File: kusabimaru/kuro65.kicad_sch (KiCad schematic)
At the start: 23 parts, among them IC1 ATMEGA32U4, J1 ISP, J2 USB4085-GF-A, SW1 SW_RESET, Y1 16MHz

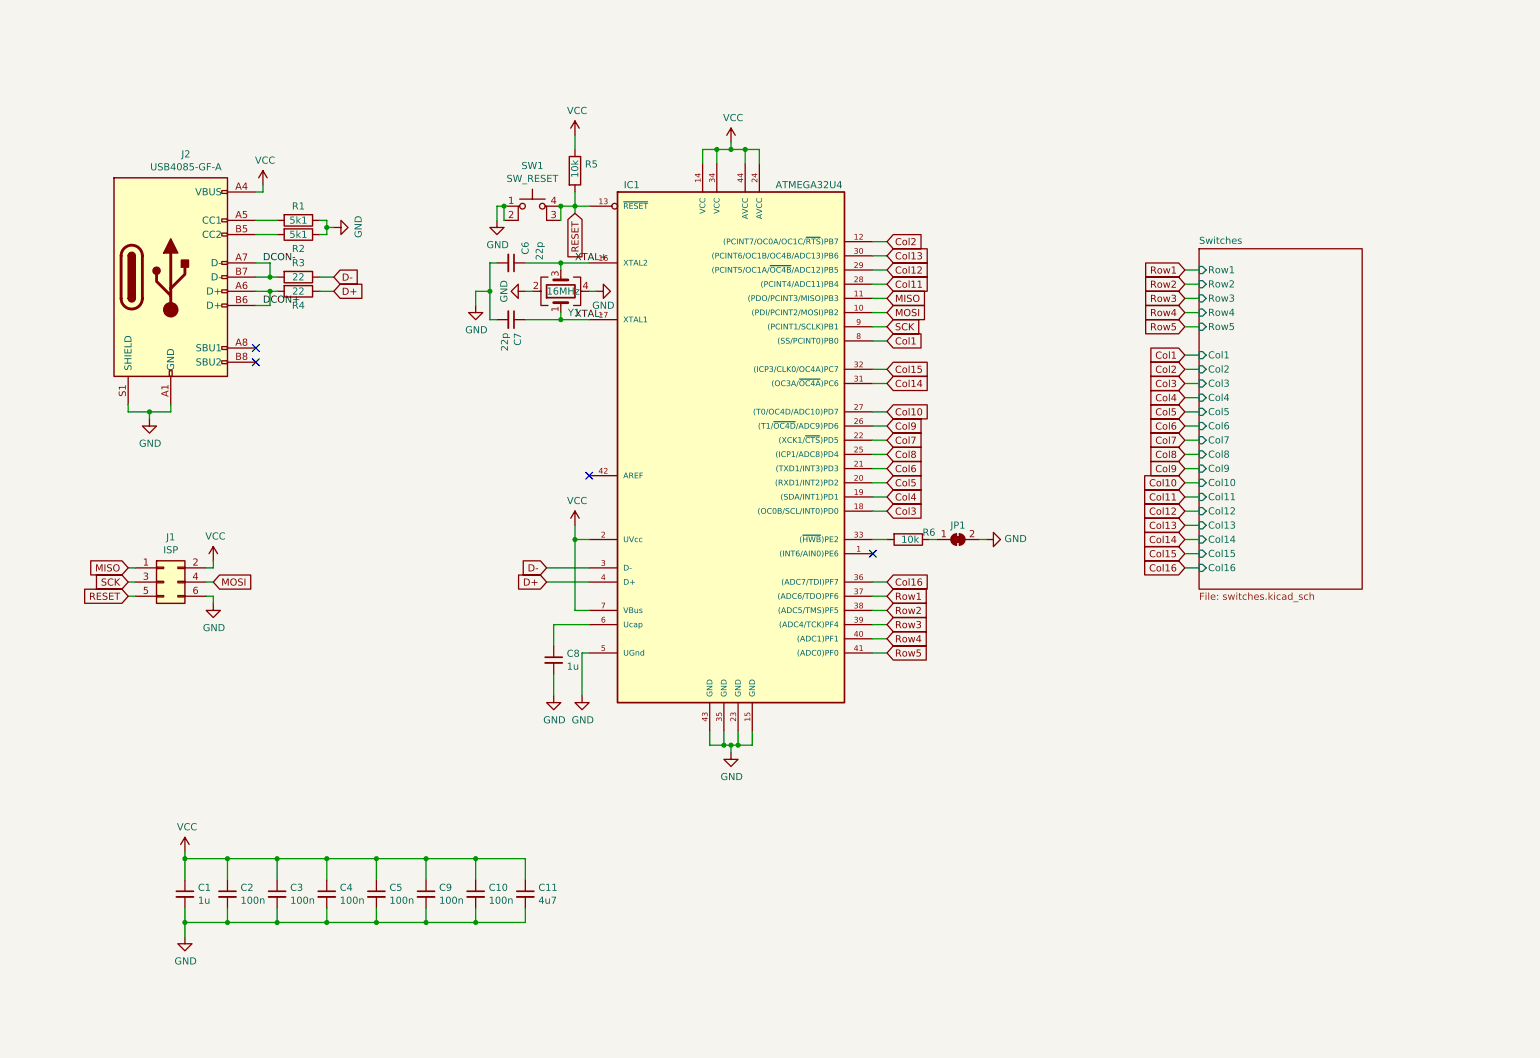
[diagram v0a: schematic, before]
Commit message: Changed schematic and PCB layout for kuro65. Routing of PCB is incomplete.
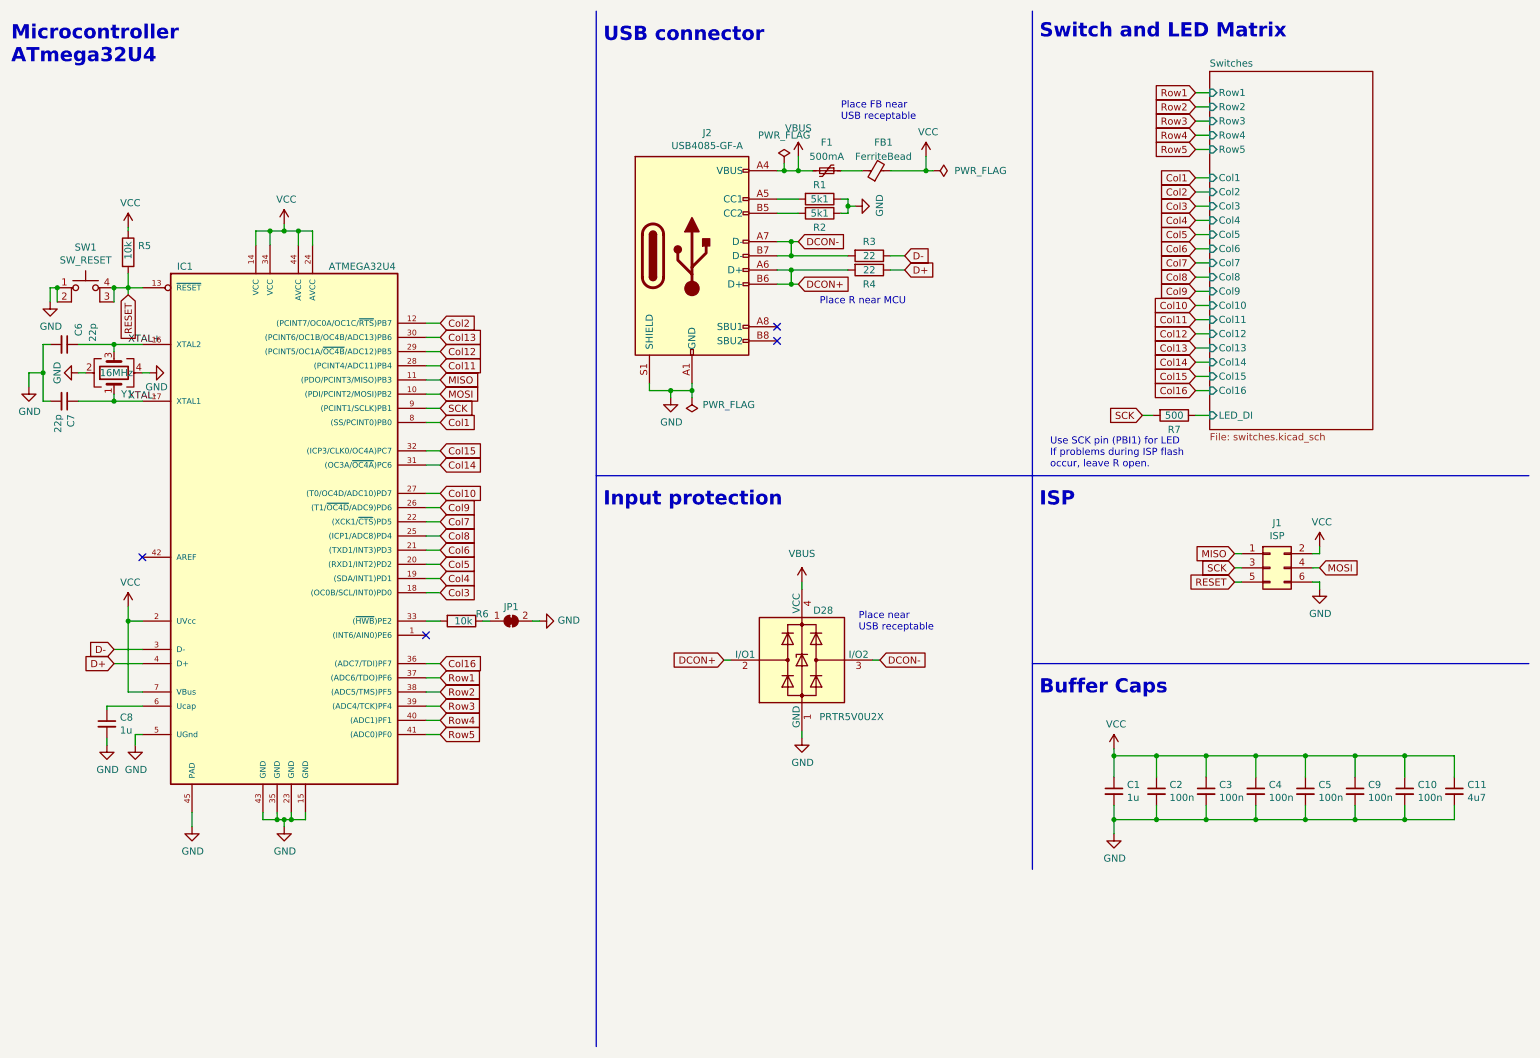
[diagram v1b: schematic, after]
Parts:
- added D28: PRTR5V0U2X, Package_TO_SOT_SMD:SOT-143, symbol Power_Protection:PRTR5V0U2X
- added F1: 500mA, Fuse:Fuse_0603_1608Metric_Pad1.05x0.95mm_HandSolder, symbol Device:Polyfuse_Small
- added FB1: FerriteBead, Resistor_SMD:R_0805_2012Metric_Pad1.20x1.40mm_HandSolder, symbol Device:FerriteBead_Small
- added R7: 500, Resistor_SMD:R_0603_1608Metric_Pad0.98x0.95mm_HandSolder, symbol Device:R
- C1, C10, C11, C2, C3, C4, C5, C6, C7, C8, C9: footprint Capacitor_SMD:C_0805_2012Metric_Pad1.18x1.45mm_HandSolder -> Capacitor_SMD:C_0603_1608Metric_Pad1.08x0.95mm_HandSolder
- IC1: footprint Package_QFP:TQFP-44_10x10mm_P0.8mm -> TM_qfn:QFN-44-1EP_7x7mm_P0.5mm_EP5.2x5.2mm_hand_solder
- R1, R2, R3, R4, R5, R6: footprint Resistor_SMD:R_0805_2012Metric_Pad1.20x1.40mm_HandSolder -> Resistor_SMD:R_0603_1608Metric_Pad0.98x0.95mm_HandSolder
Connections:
- net DCON+: now also D28.2 (I/O1)
- net DCON-: now also D28.3 (I/O2)
- net GND: now also IC1.45 (PAD), D28.1 (GND)
- net SCK: now also R7.2
- net VCC: now also FB1.2; no longer J2.A4 (VBUS), J2.A9 (VBUS), J2.B4 (VBUS), J2.B9 (VBUS)
- new net: F1.1, FB1.1
- new net Switches/LED_DI: R7.1
- new net VBUS: D28.4 (VCC), F1.2, J2.A4 (VBUS), J2.A9 (VBUS), J2.B4 (VBUS), J2.B9 (VBUS)
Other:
- sheet Switches ports: added LED_DI; removed none
- note added: "Buffer Caps"
- note added: "ISP"
- note added: "Input protection"
- note added: "Microcontroller ATmega32U4"
- note added: "Place FB near USB receptable"
- note added: "Place R near MCU"
- note added: "Place near USB receptable"
- note added: "Switch and LED Matrix"
- note added: "USB connector"
- note added: "Use SCK pin (PBI1) for LED If problems during ISP flash occur, leave R open."
- moved on the sheet: C1, C10, C11, C2, C3, C4, C5, C6, C7, C8, C9, J1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

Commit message: Updated PCB layout for DZ65 compatibility.
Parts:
- added IC2: ATMEGA32U4, Package_QFP:LQFP-44_10x10mm_P0.8mm, symbol atmega32u4:ATMEGA32U4
- IC1: footprint TM_qfn:QFN-44-1EP_7x7mm_P0.5mm_EP5.2x5.2mm_hand_solder -> Package_DFN_QFN:QFN-44-1EP_7x7mm_P0.5mm_EP5.2x5.2mm_ThermalVias
- J2: value USB4085-GF-A -> USB TYPE-C-31-M-12; footprint Connector_USB:USB_C_Receptacle_GCT_USB4085 -> Connector_USB:USB_C_Receptacle_HRO_TYPE-C-31-M-12; Shop-URL https://www.digikey.de/product-detail/de/gct/USB4085-GF-A/2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 -> https://jlcpcb.com/partdetail/Korean_HropartsElec-TYPE_C_31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
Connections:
- net Col1: now also IC2.8 ((SS/PCINT0)PB0)
- net Col10: now also IC2.27 ((T0/OC4D/ADC10)PD7)
- net Col11: now also IC2.28 ((PCINT4/ADC11)PB4)
- net Col12: now also IC2.29 ((PCINT5/OC1A/~{OC4B}/ADC12)PB5)
- net Col13: now also IC2.30 ((PCINT6/OC1B/OC4B/ADC13)PB6)
- net Col14: now also IC2.31 ((OC3A/~{OC4A})PC6)
- net Col15: now also IC2.32 ((ICP3/CLK0/OC4A)PC7)
- net Col16: now also IC2.36 ((ADC7/TDI)PF7)
- net Col2: now also IC2.12 ((PCINT7/OC0A/OC1C/~{RTS})PB7)
- net Col3: now also IC2.18 ((OC0B/SCL/INT0)PD0)
- net Col4: now also IC2.19 ((SDA/INT1)PD1)
- net Col5: now also IC2.20 ((RXD1/INT2)PD2)
- net Col6: now also IC2.21 ((TXD1/INT3)PD3)
- net Col7: now also IC2.22 ((XCK1/~{CTS})PD5)
- net Col8: now also IC2.25 ((ICP1/ADC8)PD4)
- net Col9: now also IC2.26 ((T1/~{OC4D}/ADC9)PD6)
- net D+: now also IC2.4 (D+)
- net D-: now also IC2.3 (D-)
- net GND: now also IC2.15 (GND), IC2.23 (GND), IC2.35 (GND), IC2.43 (GND), IC2.45 (PAD), IC2.5 (UGnd)
- net MISO: now also IC2.11 ((PDO/PCINT3/MISO)PB3)
- net MOSI: now also IC2.10 ((PDI/PCINT2/MOSI)PB2)
- net RESET: now also IC2.13 (~{RESET})
- net Row1: now also IC2.37 ((ADC6/TDO)PF6)
- net Row2: now also IC2.38 ((ADC5/TMS)PF5)
- net Row3: now also IC2.39 ((ADC4/TCK)PF4)
- net Row4: now also IC2.40 ((ADC1)PF1)
- net Row5: now also IC2.41 ((ADC0)PF0)
- net SCK: now also IC2.9 ((PCINT1/SCLK)PB1)
- net VCC: now also IC2.14 (VCC), IC2.2 (UVcc), IC2.24 (AVCC), IC2.34 (VCC), IC2.44 (AVCC), IC2.7 (VBus)
- net XTAL+: now also IC2.16 (XTAL2)
- net XTAL-: now also IC2.17 (XTAL1)
- net at IC1.1 ((INT6/AIN0)PE6): now also IC2.1 ((INT6/AIN0)PE6)
- net at IC1.33 ((~{HWB})PE2), R6.2: now also IC2.33 ((~{HWB})PE2)
- net at IC1.42 (AREF): now also IC2.42 (AREF)
- net at C8.1, IC1.6 (Ucap): now also IC2.6 (Ucap)
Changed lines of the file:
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@@
     (company "0x544D")
   )
+  (junction (at 87.63 113.665) (diameter 0) (color 0 0 0 0)
+  )
+  (junction (at 87.63 128.905) (diameter 0) (color 0 0 0 0)
+  )
+  (junction (at 87.63 141.605) (diameter 0) (color 0 0 0 0)
+  )
   (junction (at 131.445 80.01) (diameter 0) (color 0 0 0 0)
   )
   (junction (at 59.69 51.435) (diameter 0) (color 0 0 0 0)
   )
+  (junction (at 87.63 136.525) (diameter 0) (color 0 0 0 0)
+  )
   (junction (at 62.23 156.845) (diameter 0) (color 0 0 0 0)
   )
@@
   (junction (at 236.22 145.415) (diameter 0) (color 0 0 0 0)
   )
+  (junction (at 87.63 139.065) (diameter 0) (color 0 0 0 0)
+  )
   (junction (at 135.255 80.01) (diameter 0) (color 0 0 0 0)
   )
   (junction (at 236.22 156.845) (diameter 0) (color 0 0 0 0)
   )
+  (junction (at 87.63 116.205) (diameter 0) (color 0 0 0 0)
+  )
   (junction (at 63.5 156.845) (diameter 0) (color 0 0 0 0)
   )
@@
   (junction (at 34.29 121.285) (diameter 0) (color 0 0 0 0)
   )
+  (junction (at 87.63 108.585) (diameter 0) (color 0 0 0 0)
+  )
   (junction (at 153.035 53.34) (diameter 0) (color 0 0 0 0)
   )
   (junction (at 254 145.415) (diameter 0) (color 0 0 0 0)
   )
+  (junction (at 87.63 131.445) (diameter 0) (color 0 0 0 0)
+  )
   (junction (at 31.75 61.595) (diameter 0) (color 0 0 0 0)
   )
+  (junction (at 87.63 121.285) (diameter 0) (color 0 0 0 0)
+  )
   (junction (at 21.59 61.595) (diameter 0) (color 0 0 0 0)
   )
@@
   (junction (at 227.33 145.415) (diameter 0) (color 0 0 0 0)
   )
+  (junction (at 87.63 133.985) (diameter 0) (color 0 0 0 0)
+  )
   (junction (at 153.035 58.42) (diameter 0) (color 0 0 0 0)
   )
   (junction (at 218.44 145.415) (diameter 0) (color 0 0 0 0)
   )
+  (junction (at 87.63 106.045) (diameter 0) (color 0 0 0 0)
+  )
   (junction (at 163.195 46.99) (diameter 0) (color 0 0 0 0)
   )
@@
   (junction (at 262.89 145.415) (diameter 0) (color 0 0 0 0)
   )
+  (junction (at 87.63 111.125) (diameter 0) (color 0 0 0 0)
+  )
   (junction (at 254 156.845) (diameter 0) (color 0 0 0 0)
   )
@@
     (property "Reference" "IC1" (id 0) (at 44.45 57.785 0))
     (property "Value" "ATMEGA32U4" (id 1) (at 76.2 57.785 0))
-    (property "Footprint" "TM_qfn:QFN-44-1EP_7x7mm_P0.5mm_EP5.2x5.2mm_hand_solder" (id 2) (at 74.93 154.94 0)
+    (property "Footprint" "Package_DFN_QFN:QFN-44-1EP_7x7mm_P0.5mm_EP5.2x5.2mm_ThermalVias" (id 2) (at 74.93 154.94 0)
       (effects (font (size 1.27 1.27)) hide)
     )
@@
     (in_bom yes) (on_board yes)
     (property "Reference" "J2" (id 0) (at 137.9728 33.8582 0))
-    (property "Value" "USB4085-GF-A" (id 1) (at 137.9728 36.1696 0))
-    (property "Footprint" "Connector_USB:USB_C_Receptacle_GCT_USB4085" (id 2) (at 139.065 55.88 0)
+    (property "Value" "USB TYPE-C-31-M-12" (id 1) (at 137.9728 36.1696 0))
+    (property "Footprint" "Connector_USB:USB_C_Receptacle_HRO_TYPE-C-31-M-12" (id 2) (at 139.065 55.88 0)
       (effects (font (size 1.27 1.27)) hide)
     )
@@
       (effects (font (size 1.27 1.27)) hide)
     )
-    (property "Shop-URL" "https://www.digikey.de/product-detail/de/gct/USB4085-GF-A/2073-USB4085-GF-ACT-ND/9859733" (id 4) (at 135.255 55.88 0)
+    (property "Shop-URL" "https://jlcpcb.com/partdetail/Korean_HropartsElec-TYPE_C_31_M12/C165948" (id 4) (at 135.255 55.88 0)
       (effects (font (size 1.27 1.27)) hide)
     )
@@
     (pin "1")
   )
+  (symbol (lib_id "atmega32u4:ATMEGA32U4") (at 62.23 104.775 0) (unit 1)
+    (in_bom yes) (on_board yes) (fields_autoplaced)
+    (property "Reference" "IC2" (id 0) (at 69.1897 53.34 0)
+      (effects (font (size 1.27 1.27)) (justify left))
+    )
+    (property "Value" "ATMEGA32U4" (id 1) (at 69.1897 55.88 0)
+      (effects (font (size 1.27 1.27)) (justify left))
+    )
+    (property "Footprint" "Package_QFP:LQFP-44_10x10mm_P0.8mm" (id 2) (at 74.93 154.94 0)
+      (effects (font (size 1.27 1.27)) hide)
+    )
+    (property "Datasheet" "" (id 3) (at 62.23 104.775 0)
+      (effects (font (size 1.27 1.27)) hide)
+    )
+    (pin "1")
+    (pin "10")
+    (pin "11")
+    (pin "12")
+    (pin "13")
+    (pin "14")
+    (pin "15")
+    (pin "16")
+    (pin "17")
+    (pin "18")
+    (pin "19")
+    (pin "2")
+    (pin "20")
+    (pin "21")
+    (pin "22")
+    (pin "23")
+    (pin "24")
+    (pin "25")
+    (pin "26")
+    (pin "27")
+    (pin "28")
+    (pin "29")
+    (pin "3")
+    (pin "30")
+    (pin "31")
+    (pin "32")
+    (pin "33")
+    (pin "34")
+    (pin "35")
+    (pin "36")
+    (pin "37")
+    (pin "38")
+    (pin "39")
+    (pin "4")
+    (pin "40")
+    (pin "41")
+    (pin "42")
+    (pin "43")
+    (pin "44")
+    (pin "45")
+    (pin "5")
+    (pin "6")
+    (pin "7")
+    (pin "8")
+    (pin "9")
+  )
   (symbol (lib_id "power:GND") (at 154.94 142.24 0) (unit 1)
     (in_bom yes) (on_board yes)
@@
     )
     (path "/00000000-0000-0000-0000-000060129e73"
-      (reference "IC1") (unit 1) (value "ATMEGA32U4") (footprint "TM_qfn:QFN-44-1EP_7x7mm_P0.5mm_EP5.2x5.2mm_hand_solder")
+      (reference "IC1") (unit 1) (value "ATMEGA32U4") (footprint "Package_DFN_QFN:QFN-44-1EP_7x7mm_P0.5mm_EP5.2x5.2mm_ThermalVias")
+    )
+    (path "/9667a659-5ee8-4481-a1b3-3f8925e40306"
+      (reference "IC2") (unit 1) (value "ATMEGA32U4") (footprint "Package_QFP:LQFP-44_10x10mm_P0.8mm")
     )
     (path "/00000000-0000-0000-0000-00006015878c"
@@
     )
     (path "/00000000-0000-0000-0000-0000602f27f9"
-      (reference "J2") (unit 1) (value "USB4085-GF-A") (footprint "Connector_USB:USB_C_Receptacle_GCT_USB4085")
+      (reference "J2") (unit 1) (value "USB TYPE-C-31-M-12") (footprint "Connector_USB:USB_C_Receptacle_HRO_TYPE-C-31-M-12")
     )
     (path "/00000000-0000-0000-0000-00006014eb13"

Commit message: Updates in routed PCB.
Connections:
- net SCK: no longer R7.2
- net LED_DI: now reaches IC1.1 ((INT6/AIN0)PE6), IC2.1 ((INT6/AIN0)PE6)
- net LED_DI: now also R7.2
- no-connect marks 4 -> 3
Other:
- note removed: "Use SCK pin (PBI1) for LED If problems during ISP flash occur, leave R open."
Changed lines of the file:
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@@
   (junction (at 59.69 51.435) (diameter 0) (color 0 0 0 0)
+  )
+  (junction (at 87.63 123.825) (diameter 0) (color 0 0 0 0)
   )
   (junction (at 87.63 136.525) (diameter 0) (color 0 0 0 0)
@@
   (no_connect (at 150.495 71.12))
   (no_connect (at 36.83 109.855))
-  (no_connect (at 87.63 123.825))
   (wire (pts (xy 20.32 71.755) (xy 19.05 71.755))
     (stroke (width 0) (type default) (color 0 0 0 0))
@@
   )
   (wire (pts (xy 20.32 81.915) (xy 19.05 81.915))
+    (stroke (width 0) (type default) (color 0 0 0 0))
+  )
+  (wire (pts (xy 87.63 123.825) (xy 90.17 123.825))
     (stroke (width 0) (type default) (color 0 0 0 0))
   )
@@
     (effects (font (size 1.27 1.27)) (justify left bottom))
   )
-  (text "Use SCK pin (PBI1) for LED\nIf problems during ISP flash\noccur, leave R open."
-    (at 199.39 93.98 0)
-    (effects (font (size 1.27 1.27)) (justify left bottom))
-  )
   (text "Microcontroller\nATmega32U4" (at 13.335 21.59 0)
     (effects (font (size 2.54 2.54) (thickness 0.508) bold) (justify left bottom))
@@
     )
   )
+  (global_label "LED_DI" (shape input) (at 215.9 84.455 180) (fields_autoplaced)
+    (effects (font (size 1.27 1.27)) (justify right))
+    (property "Intersheet References" "${INTERSHEET_REFS}" (id 0) (at 207.2863 84.5344 0)
+      (effects (font (size 1.27 1.27)) (justify right) hide)
+    )
+  )
   (global_label "Row3" (shape input) (at 90.17 136.525 0) (fields_autoplaced)
     (effects (font (size 1.27 1.27)) (justify left))
@@
     )
   )
+  (global_label "LED_DI" (shape input) (at 90.17 123.825 0) (fields_autoplaced)
+    (effects (font (size 1.27 1.27)) (justify left))
+    (property "Intersheet References" "${INTERSHEET_REFS}" (id 0) (at 98.7837 123.7456 0)
+      (effects (font (size 1.27 1.27)) (justify left) hide)
+    )
+  )
   (global_label "Col6" (shape input) (at 225.425 54.61 180) (fields_autoplaced)
     (effects (font (size 1.27 1.27)) (justify right))
@@
       (effects (font (size 1.27 1.27)) hide)
     )
-  )
-  (global_label "SCK" (shape input) (at 215.9 84.455 180) (fields_autoplaced)
-    (effects (font (size 1.27 1.27)) (justify right))
-    (property "Intersheet References" "${INTERSHEET_REFS}" (id 0) (at 181.61 -29.845 0)
-      (effects (font (size 1.27 1.27)) hide)
-    )
